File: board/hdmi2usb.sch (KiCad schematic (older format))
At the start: 0 parts

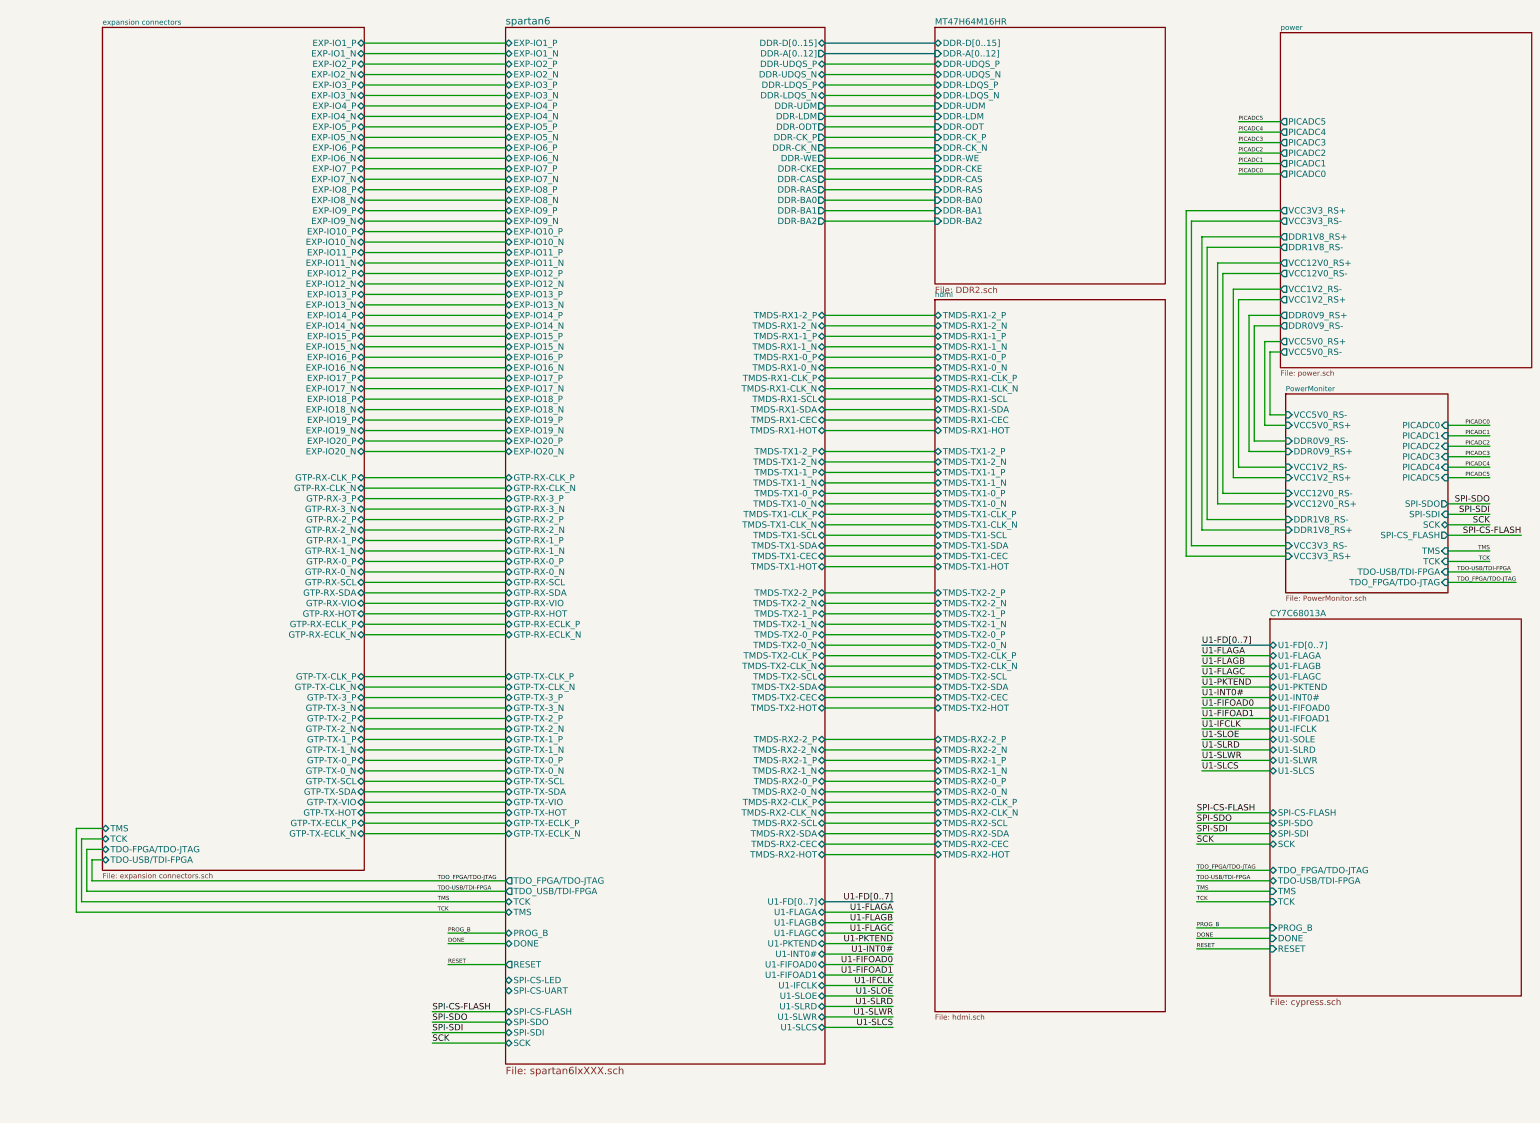
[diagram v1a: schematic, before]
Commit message: Issue #1022 - Reset signals
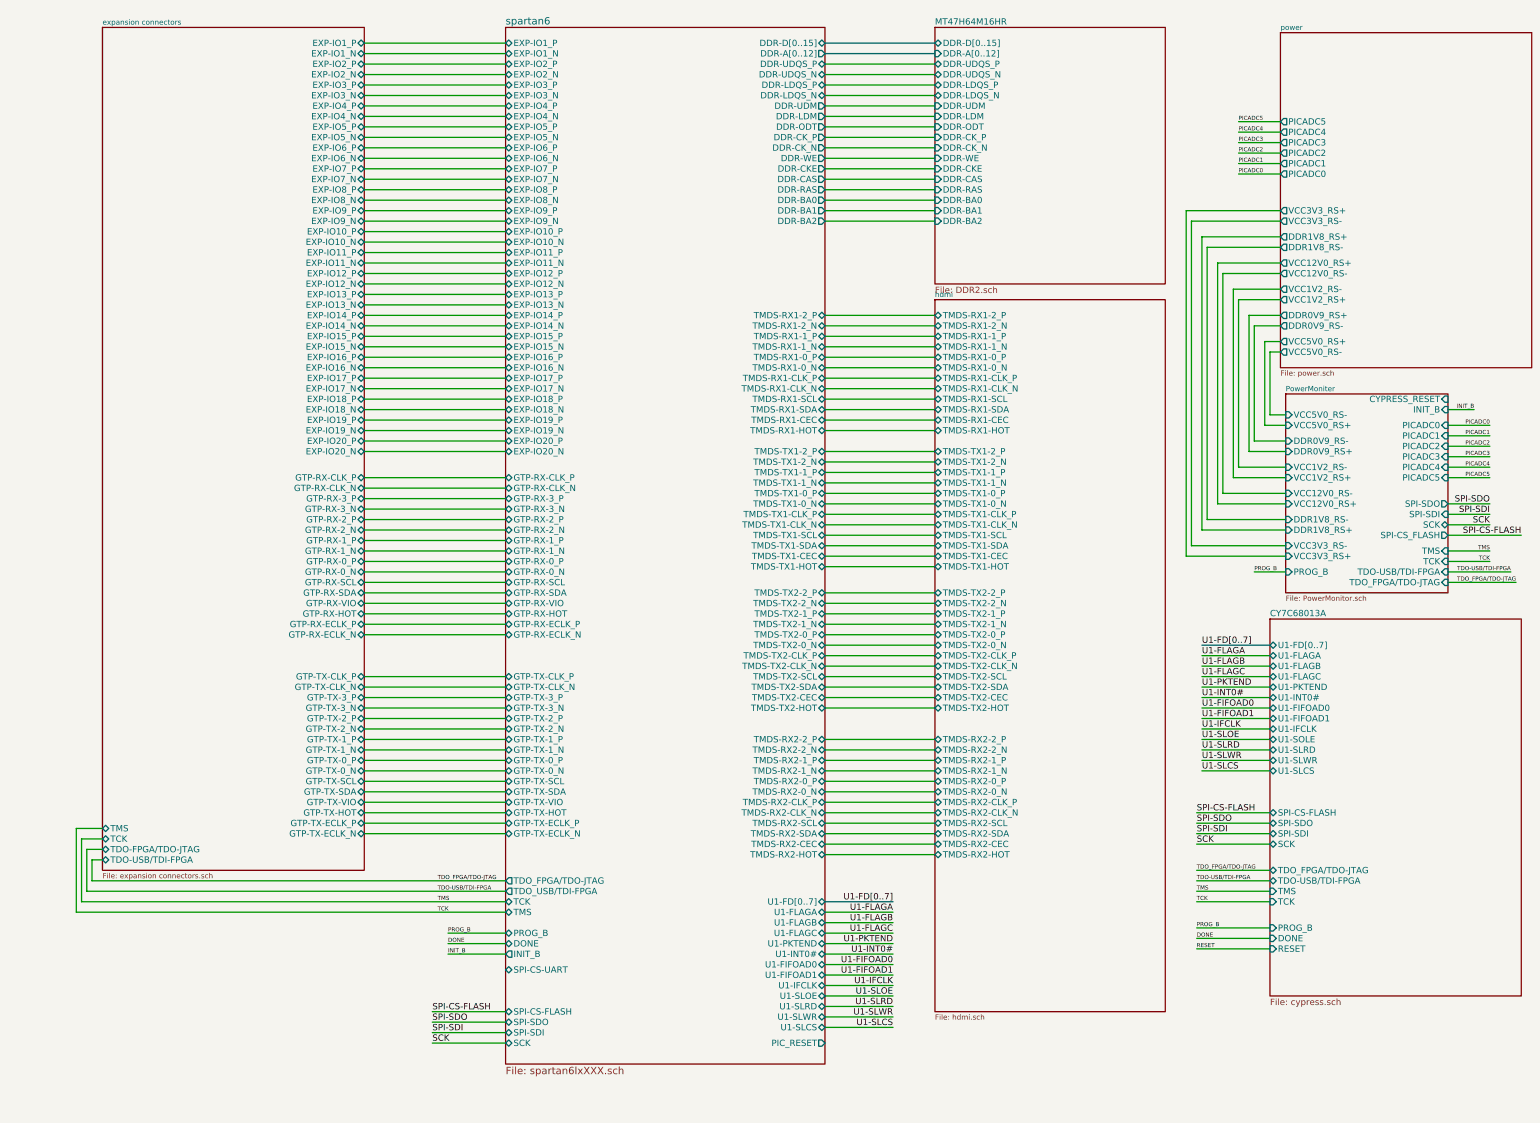
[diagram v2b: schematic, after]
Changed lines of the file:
@@
 Sheet 1 8
 Title ""
-Date "18 mar 2014"
+Date "25 mar 2014"
 Rev ""
 Comp ""
@@
 F26 "TDO-USB/TDI-FPGA" I R 14600 5900 60
 F27 "TDO_FPGA/TDO-JTAG" I R 14600 6000 60
+F28 "PROG_B" I L 13050 5900 60
+F29 "INIT_B" I R 14600 4350 60
+F30 "CYPRESS_RESET" I R 14600 4250 60
 $EndSheet
 Wire Wire Line
@@
 F118 "U1-FIFOAD1" B R 8650 9750 60
 F119 "U1-SLWR" B R 8650 10150 60
-F120 "SPI-CS-LED" B L 5600 9800 60
-F121 "SPI-CS-UART" B L 5600 9900 60
-F122 "SPI-SDO" B L 5600 10200 60
-F123 "SPI-SDI" B L 5600 10300 60
-F124 "SPI-CS-FLASH" B L 5600 10100 60
-F125 "GTP-RX-CLK_N" B L 5600 5100 60
-F126 "GTP-RX-0_N" B L 5600 5900 60
-F127 "GTP-RX-1_N" B L 5600 5700 60
-F128 "GTP-RX-2_N" B L 5600 5500 60
-F129 "GTP-RX-2_P" B L 5600 5400 60
-F130 "GTP-RX-3_N" B L 5600 5300 60
-F131 "GTP-RX-VIO" B L 5600 6200 60
-F132 "GTP-RX-HOT" B L 5600 6300 60
-F133 "GTP-RX-SCL" B L 5600 6000 60
-F134 "GTP-RX-SDA" B L 5600 6100 60
-F135 "GTP-TX-CLK_P" B L 5600 6900 60
-F136 "GTP-TX-CLK_N" B L 5600 7000 60
-F137 "GTP-RX-ECLK_N" B L 5600 6500 60
-F138 "GTP-RX-ECLK_P" B L 5600 6400 60
-F139 "GTP-TX-0_N" B L 5600 7800 60
-F140 "GTP-TX-0_P" B L 5600 7700 60
-F141 "GTP-TX-1_P" B L 5600 7500 60
-F142 "GTP-TX-1_N" B L 5600 7600 60
-F143 "GTP-TX-2_P" B L 5600 7300 60
-F144 "GTP-TX-2_N" B L 5600 7400 60
-F145 "GTP-TX-3_P" B L 5600 7100 60
-F146 "GTP-TX-3_N" B L 5600 7200 60
-F147 "GTP-TX-VIO" B L 5600 8100 60
-F148 "GTP-TX-HOT" B L 5600 8200 60
-F149 "GTP-TX-SCL" B L 5600 7900 60
-F150 "GTP-TX-SDA" B L 5600 8000 60
-F151 "GTP-TX-ECLK_N" B L 5600 8400 60
-F152 "GTP-RX-CLK_P" B L 5600 5000 60
-F153 "GTP-RX-1_P" B L 5600 5600 60
-F154 "GTP-RX-3_P" B L 5600 5200 60
-F155 "DONE" B L 5600 9450 60
-F156 "GTP-RX-0_P" B L 5600 5800 60
-F157 "GTP-TX-ECLK_P" B L 5600 8300 60
-F158 "U1-FIFOAD0" B R 8650 9650 60
-F159 "U1-IFCLK" B R 8650 9850 60
-F160 "U1-FLAGA" B R 8650 9150 60
-F161 "U1-SLOE" B R 8650 9950 60
-F162 "U1-SLRD" B R 8650 10050 60
-F163 "PROG_B" B L 5600 9350 60
-F164 "TDO_USB/TDI-FPGA" O L 5600 8950 60
-F165 "RESET" O L 5600 9650 60
+F120 "SPI-SDO" B L 5600 10200 60
+F121 "SPI-SDI" B L 5600 10300 60
+F122 "SPI-CS-FLASH" B L 5600 10100 60
+F123 "GTP-RX-CLK_N" B L 5600 5100 60
+F124 "GTP-RX-0_N" B L 5600 5900 60
+F125 "GTP-RX-1_N" B L 5600 5700 60
+F126 "GTP-RX-2_N" B L 5600 5500 60
+F127 "GTP-RX-2_P" B L 5600 5400 60
+F128 "GTP-RX-3_N" B L 5600 5300 60
+F129 "GTP-RX-VIO" B L 5600 6200 60
+F130 "GTP-RX-HOT" B L 5600 6300 60
+F131 "GTP-RX-SCL" B L 5600 6000 60
+F132 "GTP-RX-SDA" B L 5600 6100 60
+F133 "GTP-TX-CLK_P" B L 5600 6900 60
+F134 "GTP-TX-CLK_N" B L 5600 7000 60
+F135 "GTP-RX-ECLK_N" B L 5600 6500 60
+F136 "GTP-RX-ECLK_P" B L 5600 6400 60
+F137 "GTP-TX-0_N" B L 5600 7800 60
+F138 "GTP-TX-0_P" B L 5600 7700 60
+F139 "GTP-TX-1_P" B L 5600 7500 60
+F140 "GTP-TX-1_N" B L 5600 7600 60
+F141 "GTP-TX-2_P" B L 5600 7300 60
+F142 "GTP-TX-2_N" B L 5600 7400 60
+F143 "GTP-TX-3_P" B L 5600 7100 60
+F144 "GTP-TX-3_N" B L 5600 7200 60
+F145 "GTP-TX-VIO" B L 5600 8100 60
+F146 "GTP-TX-HOT" B L 5600 8200 60
+F147 "GTP-TX-SCL" B L 5600 7900 60
+F148 "GTP-TX-SDA" B L 5600 8000 60
+F149 "GTP-TX-ECLK_N" B L 5600 8400 60
+F150 "GTP-RX-CLK_P" B L 5600 5000 60
+F151 "GTP-RX-1_P" B L 5600 5600 60
+F152 "GTP-RX-3_P" B L 5600 5200 60
+F153 "DONE" B L 5600 9450 60
+F154 "GTP-RX-0_P" B L 5600 5800 60
+F155 "GTP-TX-ECLK_P" B L 5600 8300 60
+F156 "U1-FIFOAD0" B R 8650 9650 60
+F157 "U1-IFCLK" B R 8650 9850 60
+F158 "U1-FLAGA" B R 8650 9150 60
+F159 "U1-SLOE" B R 8650 9950 60
+F160 "U1-SLRD" B R 8650 10050 60
+F161 "PROG_B" B L 5600 9350 60
+F162 "TDO_USB/TDI-FPGA" O L 5600 8950 60
+F163 "PIC_RESET" O R 8650 10400 60
+F164 "INIT_B" O L 5600 9550 60
+F165 "SPI-CS-UART" B L 5600 9700 60
 $EndSheet
 Wire Wire Line
@@
 Wire Wire Line
 	14600 6000 15250 6000
-Wire Wire Line
-	5600 9650 5050 9650
-Text Label 5050 9650 0    39   ~ 0
-RESET
 Text Label 12200 9500 0    39   ~ 0
 RESET
@@
 Text Label 15250 6000 2    39   ~ 0
 TDO_FPGA/TDO-JTAG
+Wire Wire Line
+	5600 9550 5050 9550
+Text Label 5050 9550 0    39   ~ 0
+INIT_B
+Text Label 14850 4350 2    39   ~ 0
+INIT_B
+Wire Wire Line
+	14600 4350 14850 4350
+Text Label 12750 5900 0    39   ~ 0
+PROG_B
+Wire Wire Line
+	13050 5900 12750 5900
 $EndSCHEMATC

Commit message: Issue #1022 - Reset signals
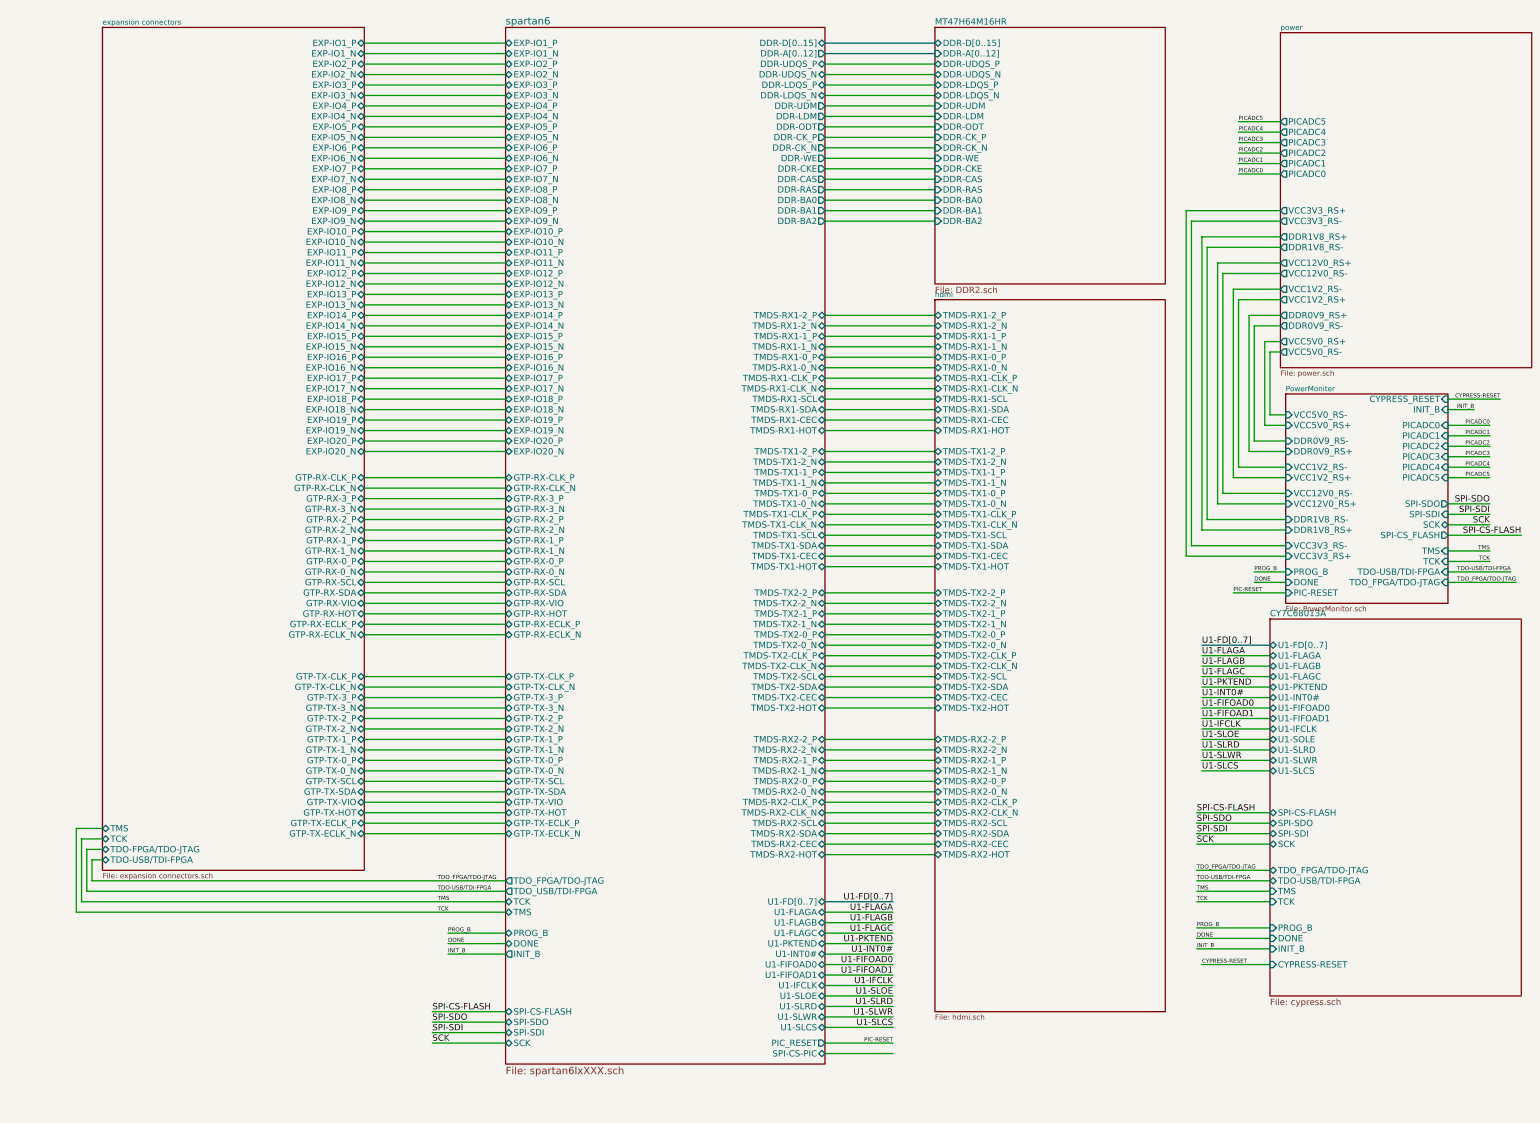
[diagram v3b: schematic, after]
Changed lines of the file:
@@
 Sheet 1 8
 Title ""
-Date "25 mar 2014"
+Date "26 mar 2014"
 Rev ""
 Comp ""
@@
 F23 "PROG_B" I L 12900 9300 60
 F24 "DONE" I L 12900 9400 60
-F25 "RESET" I L 12900 9500 60
+F25 "CYPRESS-RESET" I L 12900 9650 60
+F26 "INIT_B" I L 12900 9500 60
 $EndSheet
 $Sheet
@@
 PICADC5
 $Sheet
-S 13050 4200 1550 1900
+S 13050 4200 1550 2000
 U 530DD52A
 F0 "PowerMoniter" 50
@@
 F29 "INIT_B" I R 14600 4350 60
 F30 "CYPRESS_RESET" I R 14600 4250 60
+F31 "DONE" I L 13050 6000 60
+F32 "PIC-RESET" I L 13050 6100 60
 $EndSheet
 Wire Wire Line
@@
 F163 "PIC_RESET" O R 8650 10400 60
 F164 "INIT_B" O L 5600 9550 60
-F165 "SPI-CS-UART" B L 5600 9700 60
+F165 "SPI-CS-PIC" B R 8650 10500 60
 $EndSheet
 Wire Wire Line
@@
 Wire Wire Line
 	14600 6000 15250 6000
-Text Label 12200 9500 0    39   ~ 0
-RESET
-Wire Wire Line
-	12900 9500 12200 9500
 Text Label 15000 5250 2    60   ~ 0
 SPI-SDO
@@
 Wire Wire Line
 	13050 5900 12750 5900
+Text Label 12750 6000 0    39   ~ 0
+DONE
+Wire Wire Line
+	13050 6000 12750 6000
+Text Label 12250 9650 0    39   ~ 0
+CYPRESS-RESET
+Wire Wire Line
+	12900 9650 12250 9650
+Text Label 15100 4250 2    39   ~ 0
+CYPRESS-RESET
+Wire Wire Line
+	14600 4250 15100 4250
+Wire Wire Line
+	13050 6100 12550 6100
+Text Label 12550 6100 0    39   ~ 0
+PIC-RESET
+Text Label 12200 9500 0    39   ~ 0
+INIT_B
+Wire Wire Line
+	12900 9500 12200 9500
+Text Label 9300 10400 2    39   ~ 0
+PIC-RESET
+Wire Wire Line
+	8650 10400 9300 10400
+Wire Wire Line
+	8650 10500 9300 10500
 $EndSCHEMATC

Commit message: Issue #1022 - Schematics final.
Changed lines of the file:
@@
 Sheet 1 8
 Title ""
-Date "28 mar 2014"
+Date "31 mar 2014"
 Rev ""
 Comp ""
@@
 F21 "SPI-SDI" I R 14600 5350 60
 F22 "SCK" B R 14600 5450 60
-F23 "SPI-CS_FLASH" O R 14600 5550 60
+F23 "SPI-CS-PIC" O R 14600 5550 60
 F24 "TMS" I R 14600 5700 60
 F25 "TCK" I R 14600 5800 60
@@
 DONE
 $Sheet
-S 5600 700  3050 9900
+S 5600 700  3050 10250
 U 51AED6DE
 F0 "spartan6" 70
@@
 F161 "PROG_B" B L 5600 9350 60
 F162 "TDO_USB/TDI-FPGA" O L 5600 8950 60
-F163 "PIC_RESET" O R 8650 10400 60
+F163 "PIC_RESET" O R 8650 10550 60
 F164 "INIT_B" O L 5600 9550 60
-F165 "SPI-CS-PIC" B R 8650 10500 60
+F165 "SPI-CS-PIC" B R 8650 10650 60
+F166 "CYPRESS-RESET" B R 8650 10450 60
 $EndSheet
 Wire Wire Line
@@
 Wire Wire Line
 	14600 5450 15000 5450
-Wire Wire Line
-	14600 5550 15300 5550
 Wire Wire Line
 	14600 5700 15000 5700
@@
 Text Label 15000 5250 2    60   ~ 0
 SPI-SDO
-Text Label 15300 5550 2    60   ~ 0
-SPI-CS-FLASH
 Text Label 15000 5350 2    60   ~ 0
 SPI-SDI
@@
 Wire Wire Line
 	12900 9500 12200 9500
-Text Label 9300 10400 2    39   ~ 0
+Text Label 9300 10550 2    39   ~ 0
 PIC-RESET
 Wire Wire Line
-	8650 10400 9300 10400
-Wire Wire Line
-	8650 10500 9300 10500
+	8650 10550 9300 10550
+Wire Wire Line
+	8650 10650 9300 10650
+Text Label 9300 10450 2    39   ~ 0
+CYPRESS-RESET
+Wire Wire Line
+	8650 10450 9300 10450
+Text Label 9300 10650 2    39   ~ 0
+SPI-CS-PIC
+Text Label 15000 5550 2    39   ~ 0
+SPI-CS-PIC
+Wire Wire Line
+	14600 5550 15000 5550
 $EndSCHEMATC

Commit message: Issue #993
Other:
- note added: "CYPRESS\nCY7C68013A"
- note added: "DDR2"
- note added: "GTP/VHDCI\nEXPANSION\n"
- note added: "HDMI/DVI\n IN-OUT\nCONNECTORS"
- note added: "JTAG \nCONNECTOR\n"
- note added: "POWER \nMONITORING"
- note added: "POWER\nSUPPLY"
- note added: "SPARTAN 6\nXC6SLXXXX-CSG324"
